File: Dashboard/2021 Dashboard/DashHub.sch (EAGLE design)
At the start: 25 parts, among them J1 LEFT, J2 RIGHT, U1 ALLEGRO_MICROSYSTEMS_ACS722LL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

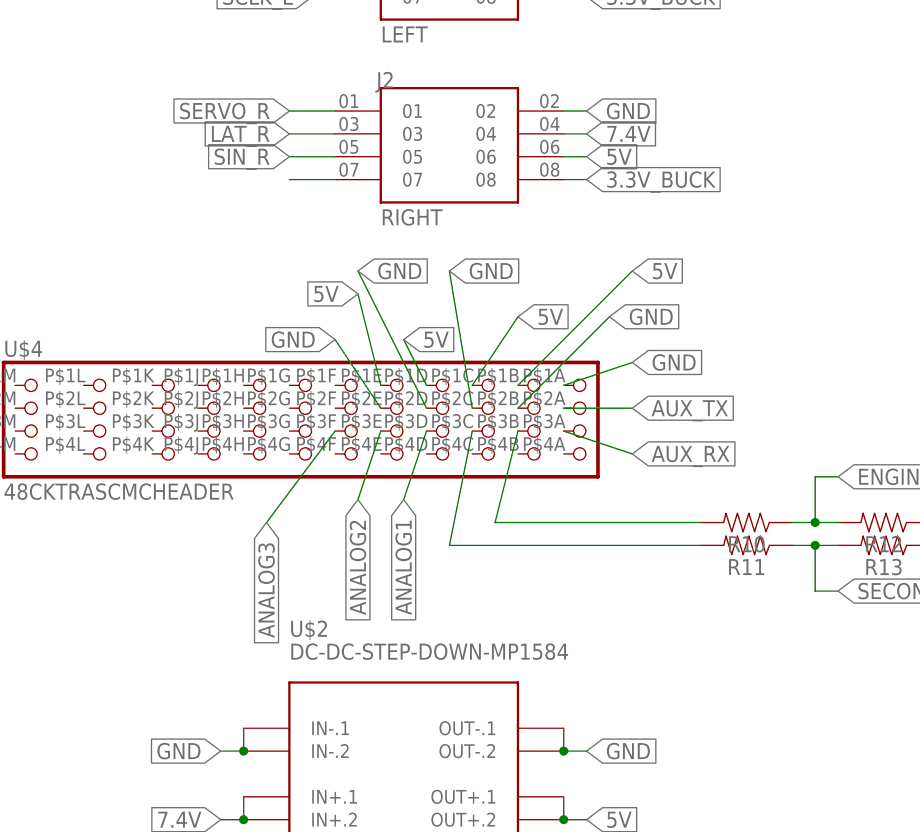
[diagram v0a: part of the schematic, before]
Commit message: Put new LED driver into dashhub
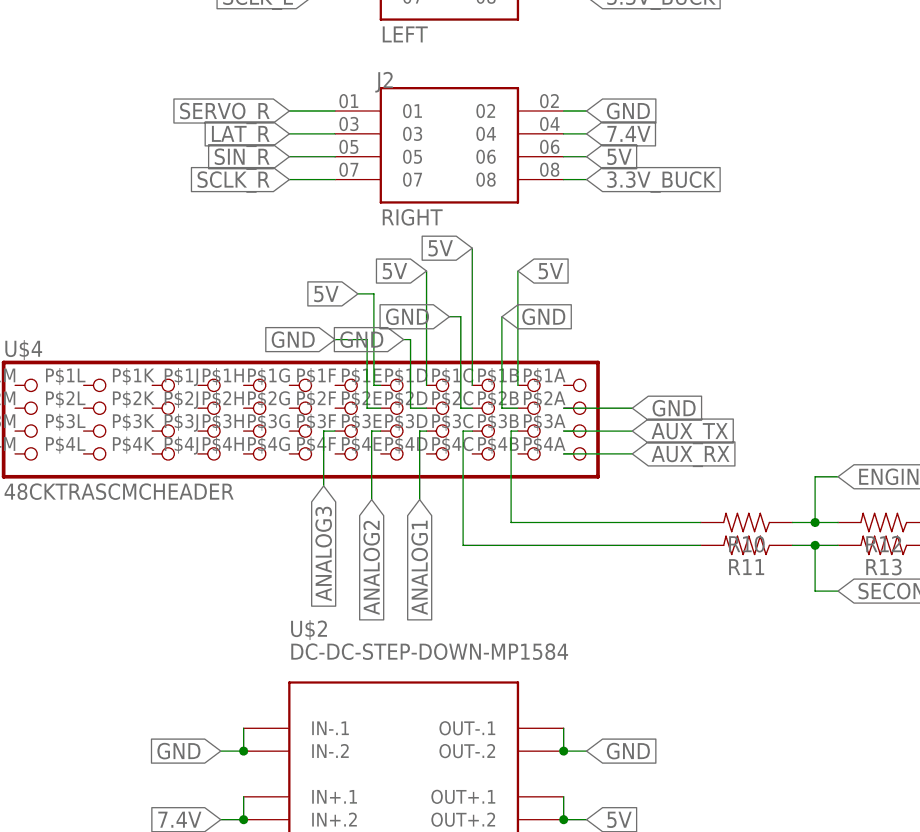
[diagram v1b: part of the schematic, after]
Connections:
- removed net N$5: U$4.1D
- removed net N$6: U$4.1E
- removed net N$7: U$4.2D
- removed net N$8: U$4.2E
- net 5V: now also U$4.1D, U$4.1E
- net AUX_RX: now also U$4.4A; no longer U$4.3A
- net AUX_TX: now also U$4.3A; no longer U$4.2A
- net GND: now also U$4.2A, U$4.2D, U$4.2E; no longer U$4.1A
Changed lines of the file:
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@@
 </segment>
 <segment>
-<wire x1="58.42" y1="30.48" x2="66.04" y2="33.02" width="0.1524" layer="91"/>
-<label x="66.04" y="33.02" size="1.778" layer="95" xref="yes"/>
-<pinref part="U$4" gate="G$1" pin="1A"/>
+<label x="66.04" y="27.94" size="1.778" layer="95" xref="yes"/>
+<wire x1="66.04" y1="27.94" x2="58.42" y2="27.94" width="0.1524" layer="91"/>
+<pinref part="U$4" gate="G$1" pin="2A"/>
 </segment>
 <segment>
@@
 </segment>
 <segment>
-<wire x1="53.34" y1="27.94" x2="63.5" y2="38.1" width="0.1524" layer="91"/>
-<label x="63.5" y="38.1" size="1.778" layer="95" xref="yes"/>
+<label x="51.562" y="38.1" size="1.778" layer="95" xref="yes"/>
 <pinref part="U$4" gate="G$1" pin="2B"/>
-</segment>
-<segment>
-<wire x1="48.26" y1="27.94" x2="45.72" y2="43.18" width="0.1524" layer="91"/>
-<label x="45.72" y="43.18" size="1.778" layer="95" xref="yes"/>
+<wire x1="53.34" y1="27.94" x2="51.562" y2="27.94" width="0.1524" layer="91"/>
+<wire x1="51.562" y1="27.94" x2="51.562" y2="38.1" width="0.1524" layer="91"/>
+</segment>
+<segment>
+<label x="45.72" y="38.1" size="1.778" layer="95" rot="MR0" xref="yes"/>
+<label x="40.64" y="35.56" size="1.778" layer="95" rot="MR0" xref="yes"/>
+<label x="33.02" y="35.56" size="1.778" layer="95" rot="R180" xref="yes"/>
 <pinref part="U$4" gate="G$1" pin="2C"/>
-<label x="35.56" y="43.18" size="1.778" layer="95" xref="yes"/>
-<label x="33.02" y="35.56" size="1.778" layer="95" rot="R180" xref="yes"/>
+<wire x1="48.26" y1="27.94" x2="46.99" y2="27.94" width="0.1524" layer="91"/>
+<wire x1="46.99" y1="27.94" x2="46.99" y2="38.1" width="0.1524" layer="91"/>
+<wire x1="46.99" y1="38.1" x2="45.72" y2="38.1" width="0.1524" layer="91"/>
+</segment>
+<segment>
+<pinref part="U$4" gate="G$1" pin="2D"/>
+<wire x1="43.18" y1="27.94" x2="41.402" y2="27.94" width="0.1524" layer="91"/>
+<wire x1="41.402" y1="27.94" x2="41.402" y2="35.56" width="0.1524" layer="91"/>
+<wire x1="40.64" y1="35.56" x2="41.402" y2="35.56" width="0.1524" layer="91"/>
+</segment>
+<segment>
+<pinref part="U$4" gate="G$1" pin="2E"/>
+<wire x1="38.1" y1="27.94" x2="36.576" y2="27.94" width="0.1524" layer="91"/>
+<wire x1="36.576" y1="27.94" x2="36.576" y2="35.56" width="0.1524" layer="91"/>
+<wire x1="36.576" y1="35.56" x2="33.02" y2="35.56" width="0.1524" layer="91"/>
 </segment>
 </net>
@@
 </segment>
 <segment>
-<wire x1="53.34" y1="30.48" x2="66.04" y2="43.18" width="0.1524" layer="91"/>
-<label x="66.04" y="43.18" size="1.778" layer="95" xref="yes"/>
+<wire x1="53.34" y1="30.48" x2="53.34" y2="43.18" width="0.1524" layer="91"/>
+<label x="53.34" y="43.18" size="1.778" layer="95" xref="yes"/>
 <pinref part="U$4" gate="G$1" pin="1B"/>
 </segment>
@@
 </segment>
 <segment>
-<wire x1="48.26" y1="30.48" x2="53.34" y2="38.1" width="0.1524" layer="91"/>
-<label x="53.34" y="38.1" size="1.778" layer="95" xref="yes"/>
+<wire x1="48.26" y1="30.48" x2="48.26" y2="45.72" width="0.1524" layer="91"/>
+<label x="48.26" y="45.72" size="1.778" layer="95" rot="MR0" xref="yes"/>
+<label x="43.18" y="43.18" size="1.778" layer="95" rot="MR0" xref="yes"/>
+<label x="35.56" y="40.64" size="1.778" layer="95" rot="R180" xref="yes"/>
 <pinref part="U$4" gate="G$1" pin="1C"/>
-<label x="40.64" y="35.56" size="1.778" layer="95" xref="yes"/>
-<label x="35.56" y="40.64" size="1.778" layer="95" rot="R180" xref="yes"/>
+</segment>
+<segment>
+<pinref part="U$4" gate="G$1" pin="1E"/>
+<wire x1="38.1" y1="30.48" x2="37.338" y2="30.48" width="0.1524" layer="91"/>
+<wire x1="37.338" y1="30.48" x2="37.338" y2="40.64" width="0.1524" layer="91"/>
+<wire x1="37.338" y1="40.64" x2="35.56" y2="40.64" width="0.1524" layer="91"/>
+</segment>
+<segment>
+<pinref part="U$4" gate="G$1" pin="1D"/>
+<wire x1="43.18" y1="30.48" x2="43.18" y2="43.18" width="0.1524" layer="91"/>
 </segment>
 </net>
@@
 </segment>
 <segment>
-<wire x1="58.42" y1="25.4" x2="66.04" y2="22.86" width="0.1524" layer="91"/>
 <label x="66.04" y="22.86" size="1.778" layer="95" xref="yes"/>
-<pinref part="U$4" gate="G$1" pin="3A"/>
+<wire x1="66.04" y1="22.86" x2="58.42" y2="22.86" width="0.1524" layer="91"/>
+<pinref part="U$4" gate="G$1" pin="4A"/>
 </segment>
 </net>
@@
 </segment>
 <segment>
-<wire x1="58.42" y1="27.94" x2="66.04" y2="27.94" width="0.1524" layer="91"/>
-<label x="66.04" y="27.94" size="1.778" layer="95" xref="yes"/>
-<pinref part="U$4" gate="G$1" pin="2A"/>
+<label x="66.04" y="25.4" size="1.778" layer="95" xref="yes"/>
+<wire x1="66.04" y1="25.4" x2="58.42" y2="25.4" width="0.1524" layer="91"/>
+<pinref part="U$4" gate="G$1" pin="3A"/>
 </segment>
 </net>
@@
 <pinref part="J2" gate="G$1" pin="07"/>
 <wire x1="33.02" y1="53.34" x2="27.94" y2="53.34" width="0.1524" layer="91"/>
+<label x="27.94" y="53.34" size="1.778" layer="95" rot="R180" xref="yes"/>
 </segment>
 </net>
@@
 <segment>
 <pinref part="R10" gate="G$1" pin="2"/>
-<wire x1="50.8" y1="15.24" x2="73.66" y2="15.24" width="0.1524" layer="91"/>
+<wire x1="52.578" y1="15.24" x2="73.66" y2="15.24" width="0.1524" layer="91"/>
+<wire x1="53.34" y1="25.4" x2="52.578" y2="25.4" width="0.1524" layer="91"/>
+<wire x1="52.578" y1="25.4" x2="52.578" y2="15.24" width="0.1524" layer="91"/>
 <pinref part="U$4" gate="G$1" pin="3B"/>
-<wire x1="50.8" y1="15.24" x2="53.34" y2="25.4" width="0.1524" layer="91"/>
 </segment>
 </net>
 <net name="N$24" class="0">
 <segment>
-<wire x1="45.72" y1="12.7" x2="73.66" y2="12.7" width="0.1524" layer="91"/>
+<wire x1="47.244" y1="12.7" x2="73.66" y2="12.7" width="0.1524" layer="91"/>
 <pinref part="R11" gate="G$1" pin="2"/>
 <pinref part="U$4" gate="G$1" pin="3C"/>
-<wire x1="45.72" y1="12.7" x2="48.26" y2="25.4" width="0.1524" layer="91"/>
+<wire x1="48.26" y1="25.4" x2="47.244" y2="25.4" width="0.1524" layer="91"/>
+<wire x1="47.244" y1="25.4" x2="47.244" y2="12.7" width="0.1524" layer="91"/>
 </segment>
 </net>
@@
 <net name="ANALOG1" class="0">
 <segment>
+<label x="42.418" y="17.78" size="1.778" layer="95" rot="R270" xref="yes"/>
 <pinref part="U$4" gate="G$1" pin="3D"/>
-<wire x1="43.18" y1="25.4" x2="40.64" y2="17.78" width="0.1524" layer="91"/>
-<label x="40.64" y="17.78" size="1.778" layer="95" rot="R270" xref="yes"/>
+<wire x1="43.18" y1="25.4" x2="42.418" y2="25.4" width="0.1524" layer="91"/>
+<wire x1="42.418" y1="25.4" x2="42.418" y2="17.78" width="0.1524" layer="91"/>
 </segment>
 <segment>
@@
 <net name="ANALOG2" class="0">
 <segment>
+<label x="37.084" y="17.78" size="1.778" layer="95" rot="R270" xref="yes"/>
 <pinref part="U$4" gate="G$1" pin="3E"/>
-<wire x1="38.1" y1="25.4" x2="35.56" y2="17.78" width="0.1524" layer="91"/>
-<label x="35.56" y="17.78" size="1.778" layer="95" rot="R270" xref="yes"/>
+<wire x1="38.1" y1="25.4" x2="37.084" y2="25.4" width="0.1524" layer="91"/>
+<wire x1="37.084" y1="25.4" x2="37.084" y2="17.78" width="0.1524" layer="91"/>
 </segment>
 <segment>
@@
 <net name="ANALOG3" class="0">
 <segment>
+<label x="31.75" y="19.304" size="1.778" layer="95" rot="R270" xref="yes"/>
 <pinref part="U$4" gate="G$1" pin="3F"/>
-<wire x1="33.02" y1="25.4" x2="25.4" y2="15.24" width="0.1524" layer="91"/>
-<label x="25.4" y="15.24" size="1.778" layer="95" rot="R270" xref="yes"/>
+<wire x1="33.02" y1="25.4" x2="31.75" y2="25.4" width="0.1524" layer="91"/>
+<wire x1="31.75" y1="25.4" x2="31.75" y2="19.304" width="0.1524" layer="91"/>
 </segment>
 <segment>
@@
 </segment>
 </net>
-<net name="N$5" class="0">
-<segment>
-<pinref part="U$4" gate="G$1" pin="1D"/>
-<wire x1="40.64" y1="35.56" x2="43.18" y2="30.48" width="0.1524" layer="91"/>
-</segment>
-</net>
-<net name="N$6" class="0">
-<segment>
-<pinref part="U$4" gate="G$1" pin="1E"/>
-<wire x1="35.56" y1="40.64" x2="38.1" y2="30.48" width="0.1524" layer="91"/>
-</segment>
-</net>
-<net name="N$7" class="0">
-<segment>
-<pinref part="U$4" gate="G$1" pin="2D"/>
-<wire x1="35.56" y1="43.18" x2="43.18" y2="27.94" width="0.1524" layer="91"/>
-</segment>
-</net>
-<net name="N$8" class="0">
-<segment>
-<pinref part="U$4" gate="G$1" pin="2E"/>
-<wire x1="33.02" y1="35.56" x2="38.1" y2="27.94" width="0.1524" layer="91"/>
-</segment>
-</net>

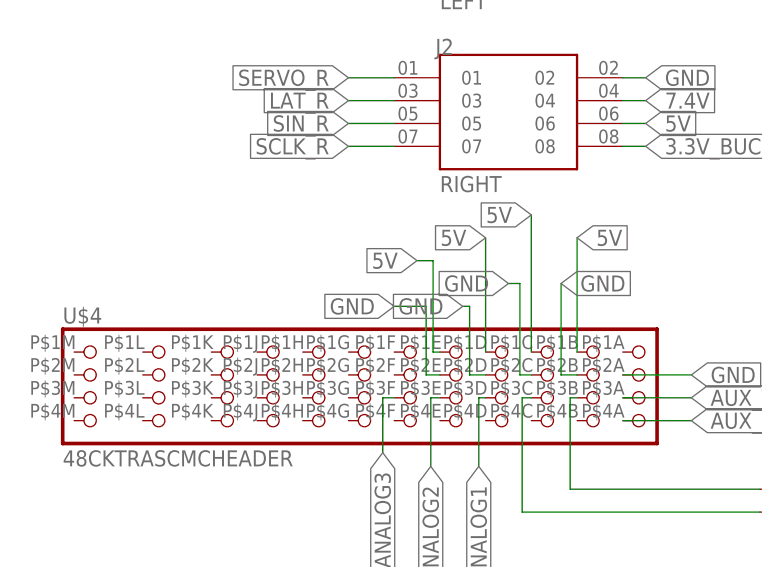
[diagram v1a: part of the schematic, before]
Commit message: More work done to dash hub and dial, gps board added
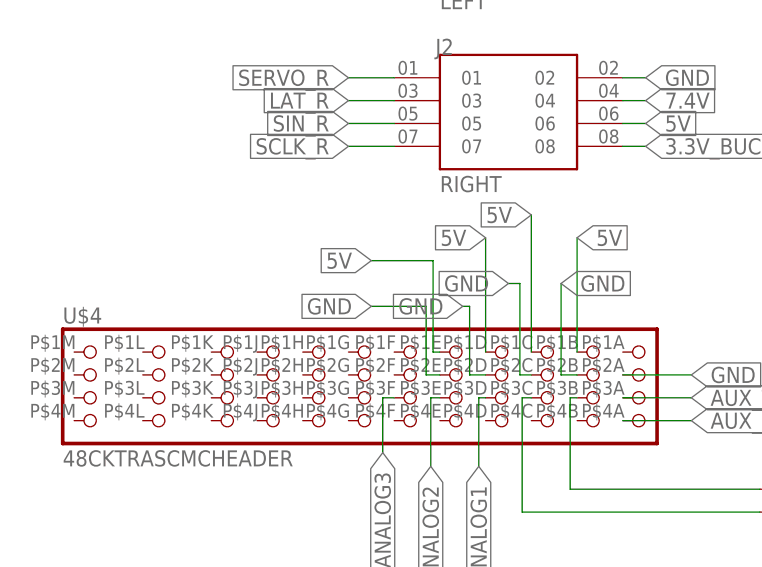
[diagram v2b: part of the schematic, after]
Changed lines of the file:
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@@
 <label x="45.72" y="38.1" size="1.778" layer="95" rot="MR0" xref="yes"/>
 <label x="40.64" y="35.56" size="1.778" layer="95" rot="MR0" xref="yes"/>
-<label x="33.02" y="35.56" size="1.778" layer="95" rot="R180" xref="yes"/>
+<label x="30.48" y="35.56" size="1.778" layer="95" rot="R180" xref="yes"/>
 <pinref part="U$4" gate="G$1" pin="2C"/>
 <wire x1="48.26" y1="27.94" x2="46.99" y2="27.94" width="0.1524" layer="91"/>
@@
 <wire x1="38.1" y1="27.94" x2="36.576" y2="27.94" width="0.1524" layer="91"/>
 <wire x1="36.576" y1="27.94" x2="36.576" y2="35.56" width="0.1524" layer="91"/>
-<wire x1="36.576" y1="35.56" x2="33.02" y2="35.56" width="0.1524" layer="91"/>
+<wire x1="36.576" y1="35.56" x2="30.48" y2="35.56" width="0.1524" layer="91"/>
 </segment>
 </net>
@@
 <label x="48.26" y="45.72" size="1.778" layer="95" rot="MR0" xref="yes"/>
 <label x="43.18" y="43.18" size="1.778" layer="95" rot="MR0" xref="yes"/>
-<label x="35.56" y="40.64" size="1.778" layer="95" rot="R180" xref="yes"/>
+<label x="30.48" y="40.64" size="1.778" layer="95" rot="R180" xref="yes"/>
 <pinref part="U$4" gate="G$1" pin="1C"/>
 </segment>
@@
 <wire x1="38.1" y1="30.48" x2="37.338" y2="30.48" width="0.1524" layer="91"/>
 <wire x1="37.338" y1="30.48" x2="37.338" y2="40.64" width="0.1524" layer="91"/>
-<wire x1="37.338" y1="40.64" x2="35.56" y2="40.64" width="0.1524" layer="91"/>
-</segment>
-<segment>
+<wire x1="37.338" y1="40.64" x2="30.48" y2="40.64" width="0.1524" layer="91"/>
+</segment>
+<segment>

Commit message: Added GPS
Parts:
- added U$5: DIYMALL_6M_GPS_BREAKOUT, GTOR - Breakout Boards:DIYMALL_6M_GPS_BREAKOUT
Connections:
- new net +3V3: U$5.VCC
- new net GPS_RX: U$5.RX
- new net GPS_TX: U$5.TX
- net GND: now also U$5.GND
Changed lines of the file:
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@@
 <part name="U$3" library="diy-modules" deviceset="DC-DC-STEP-DOWN-MP1584" device=""/>
 <part name="U$4" library="GTOR - Connectors" deviceset="48CKTRASCMCHEADER" device=""/>
+<part name="U$5" library="GTOR - Breakout Boards" deviceset="DIYMALL_6M_GPS_BREAKOUT" device=""/>
+<part name="+3V1" library="GTOR - Documation Frame" deviceset="+3V3" device=""/>
 </parts>
 <sheets>
@@
 <attribute name="NAME" x="-3.81" y="33.655" size="1.778" layer="95"/>
 <attribute name="VALUE" x="-3.81" y="17.78" size="1.778" layer="96"/>
+</instance>
+<instance part="U$5" gate="G$1" x="119.38" y="119.38" smashed="yes">
+<attribute name="NAME" x="113.03" y="127.635" size="1.778" layer="95"/>
+<attribute name="VALUE" x="113.03" y="111.76" size="1.778" layer="96"/>
+</instance>
+<instance part="+3V1" gate="G$1" x="109.22" y="129.54" smashed="yes">
+<attribute name="VALUE" x="106.68" y="124.46" size="1.778" layer="96" rot="R90"/>
 </instance>
 </instances>
@@
 <wire x1="36.576" y1="35.56" x2="30.48" y2="35.56" width="0.1524" layer="91"/>
 </segment>
+<segment>
+<label x="109.22" y="116.84" size="1.778" layer="95" rot="R180" xref="yes"/>
+<wire x1="116.84" y1="116.84" x2="109.22" y2="116.84" width="0.1524" layer="91"/>
+<pinref part="U$5" gate="G$1" pin="GND"/>
+</segment>
 </net>
 <net name="LAT_L" class="0">
@@
 <pinref part="JP2" gate="A" pin="5"/>
 <wire x1="134.62" y1="58.42" x2="129.54" y2="58.42" width="0.1524" layer="91"/>
-<wire x1="129.54" y1="58.42" x2="121.92" y2="58.42" width="0.1524" layer="91"/>
 <junction x="129.54" y="58.42"/>
-<label x="121.92" y="58.42" size="1.778" layer="95" rot="R180" xref="yes"/>
 </segment>
 </net>
@@
 <pinref part="JP2" gate="A" pin="6"/>
 <wire x1="134.62" y1="60.96" x2="129.54" y2="60.96" width="0.1524" layer="91"/>
+<junction x="129.54" y="60.96"/>
 </segment>
 </net>
@@
 </segment>
 </net>
+<net name="GPS_TX" class="0">
+<segment>
+<pinref part="U$5" gate="G$1" pin="TX"/>
+<wire x1="109.22" y1="121.92" x2="116.84" y2="121.92" width="0.1524" layer="91"/>
+<label x="109.22" y="121.92" size="1.778" layer="95" rot="R180" xref="yes"/>
+</segment>
+<segment>
+<wire x1="119.38" y1="60.96" x2="127" y2="60.96" width="0.1524" layer="91"/>
+<label x="121.92" y="60.96" size="1.778" layer="95" rot="R180" xref="yes"/>
+</segment>
+</net>
+<net name="GPS_RX" class="0">
+<segment>
+<pinref part="U$5" gate="G$1" pin="RX"/>
+<wire x1="116.84" y1="119.38" x2="109.22" y2="119.38" width="0.1524" layer="91"/>
+<label x="109.22" y="119.38" size="1.778" layer="95" rot="R180" xref="yes"/>
+</segment>
+<segment>
+<wire x1="127" y1="58.42" x2="119.38" y2="58.42" width="0.1524" layer="91"/>
+<label x="121.92" y="58.42" size="1.778" layer="95" rot="R180" xref="yes"/>
+</segment>
+</net>
+<net name="+3V3" class="0">
+<segment>
+<pinref part="U$5" gate="G$1" pin="VCC"/>
+<wire x1="116.84" y1="124.46" x2="109.22" y2="124.46" width="0.1524" layer="91"/>
+<wire x1="109.22" y1="124.46" x2="109.22" y2="127" width="0.1524" layer="91"/>
+<pinref part="+3V1" gate="G$1" pin="+3V3"/>
+</segment>
+</net>
